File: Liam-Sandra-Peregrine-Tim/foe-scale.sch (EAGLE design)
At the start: 43 parts, among them U1 LM311, U2 SAMD21E

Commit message: finished up layout. Try to place all of the names and values of th components so that they do not overlap. To do so, use the smash command by typing smash and then clicking on the component. Xs will appear next to the component name and value, and thee will appear on the silk screen. Move them around so that none overlap and so that they are right next to the component that they correspond to. You can change the size of the text in properties if need be.
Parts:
- removed U$5: LMC6482, foe-scale:LMC6482
- removed U$9: RED_LED, foe-scale:RED_LED
- added 3.3V, 5V, AGND, DGND, HYS, INA_OUT: TEST_POINT, foe-scale:TEST_POINT
- added C10, C11: 1uF, rcl:C-EUC0805K
- renumbered U$4 to SIGNAL
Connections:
- removed net TESTTESTTEST: C4.2
- net +3V3: now also 3.3V.P$1, C11.1
- net +5V: now also 5V.P$1, C10.1
- net AGND: now also AGND.P$1, C10.2, C4.2
- net DGND: now also C11.2, DGND.P$1
- net N$16: now also U$3G$2.AIN+; no longer U$5G$1.AIN+
- net N$19: now also INA_OUT.P$1, U$3G$2.OUT; no longer U$5G$1.OUT
- net N$20: now also U$3G$2.AIN-; no longer U$5G$1.AIN-
- net N$27: now also HYS.P$1
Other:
- moved on the sheet: C4

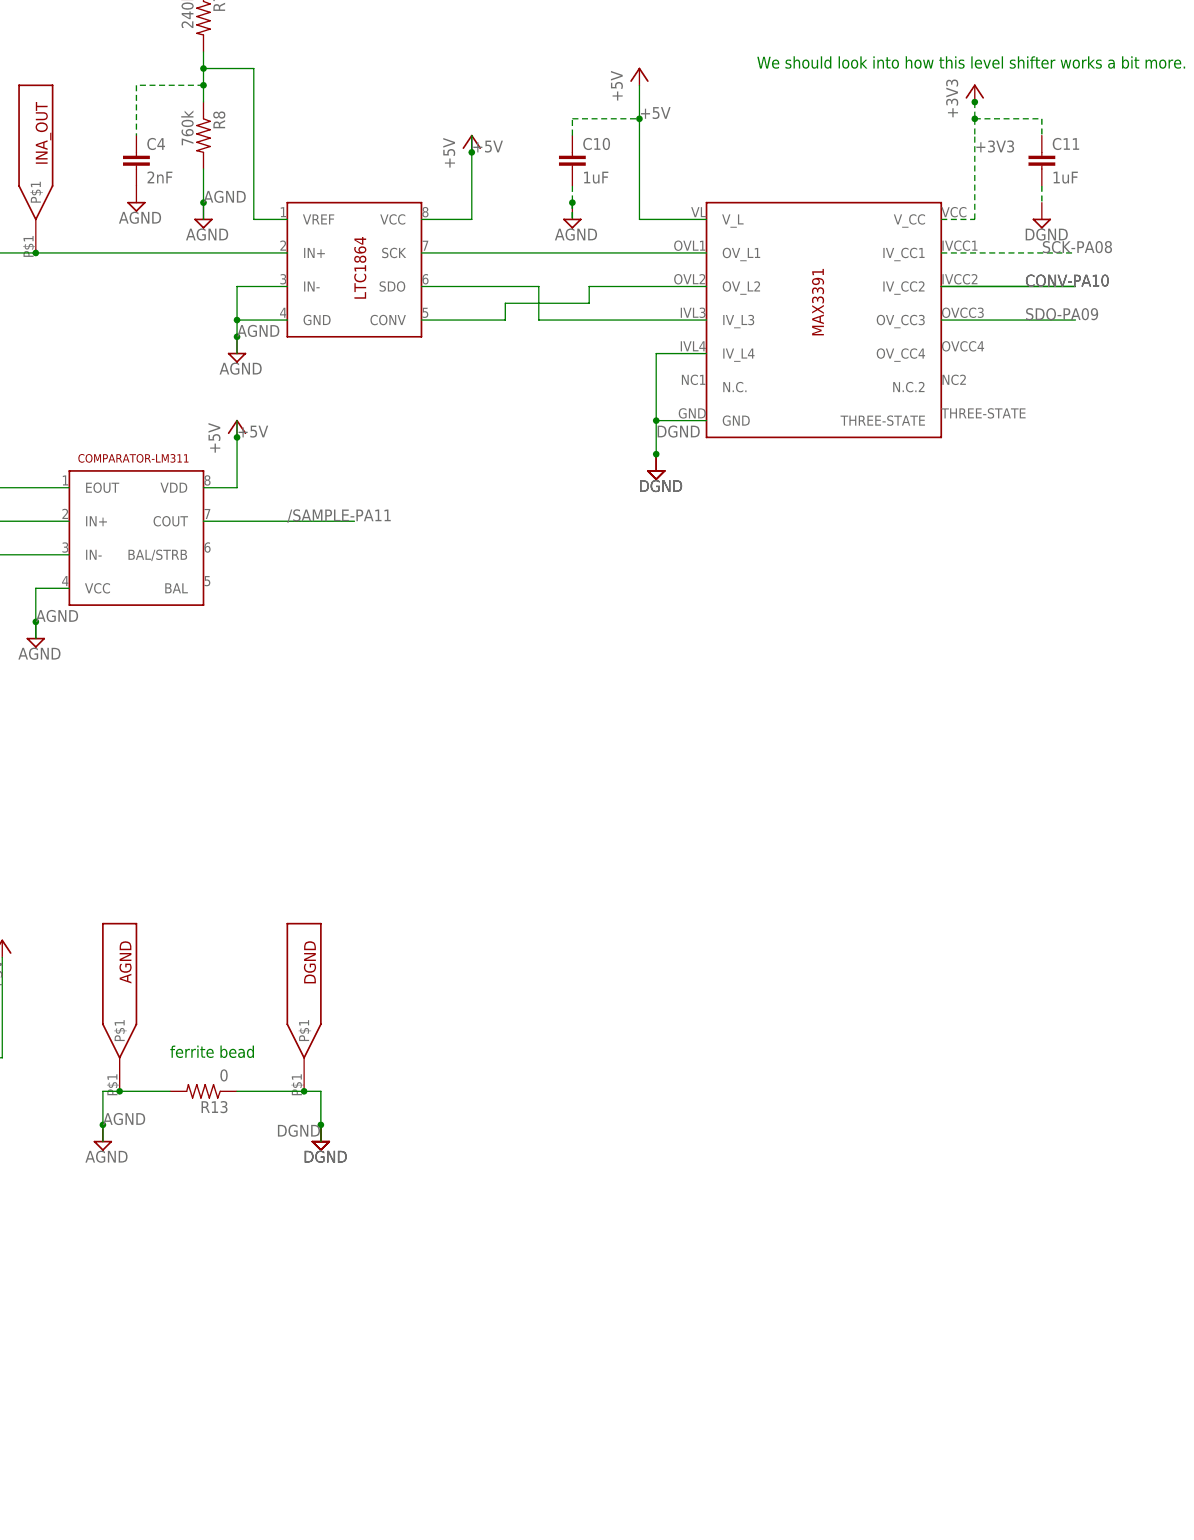
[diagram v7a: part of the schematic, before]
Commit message: replaced microUSB with standard USB B
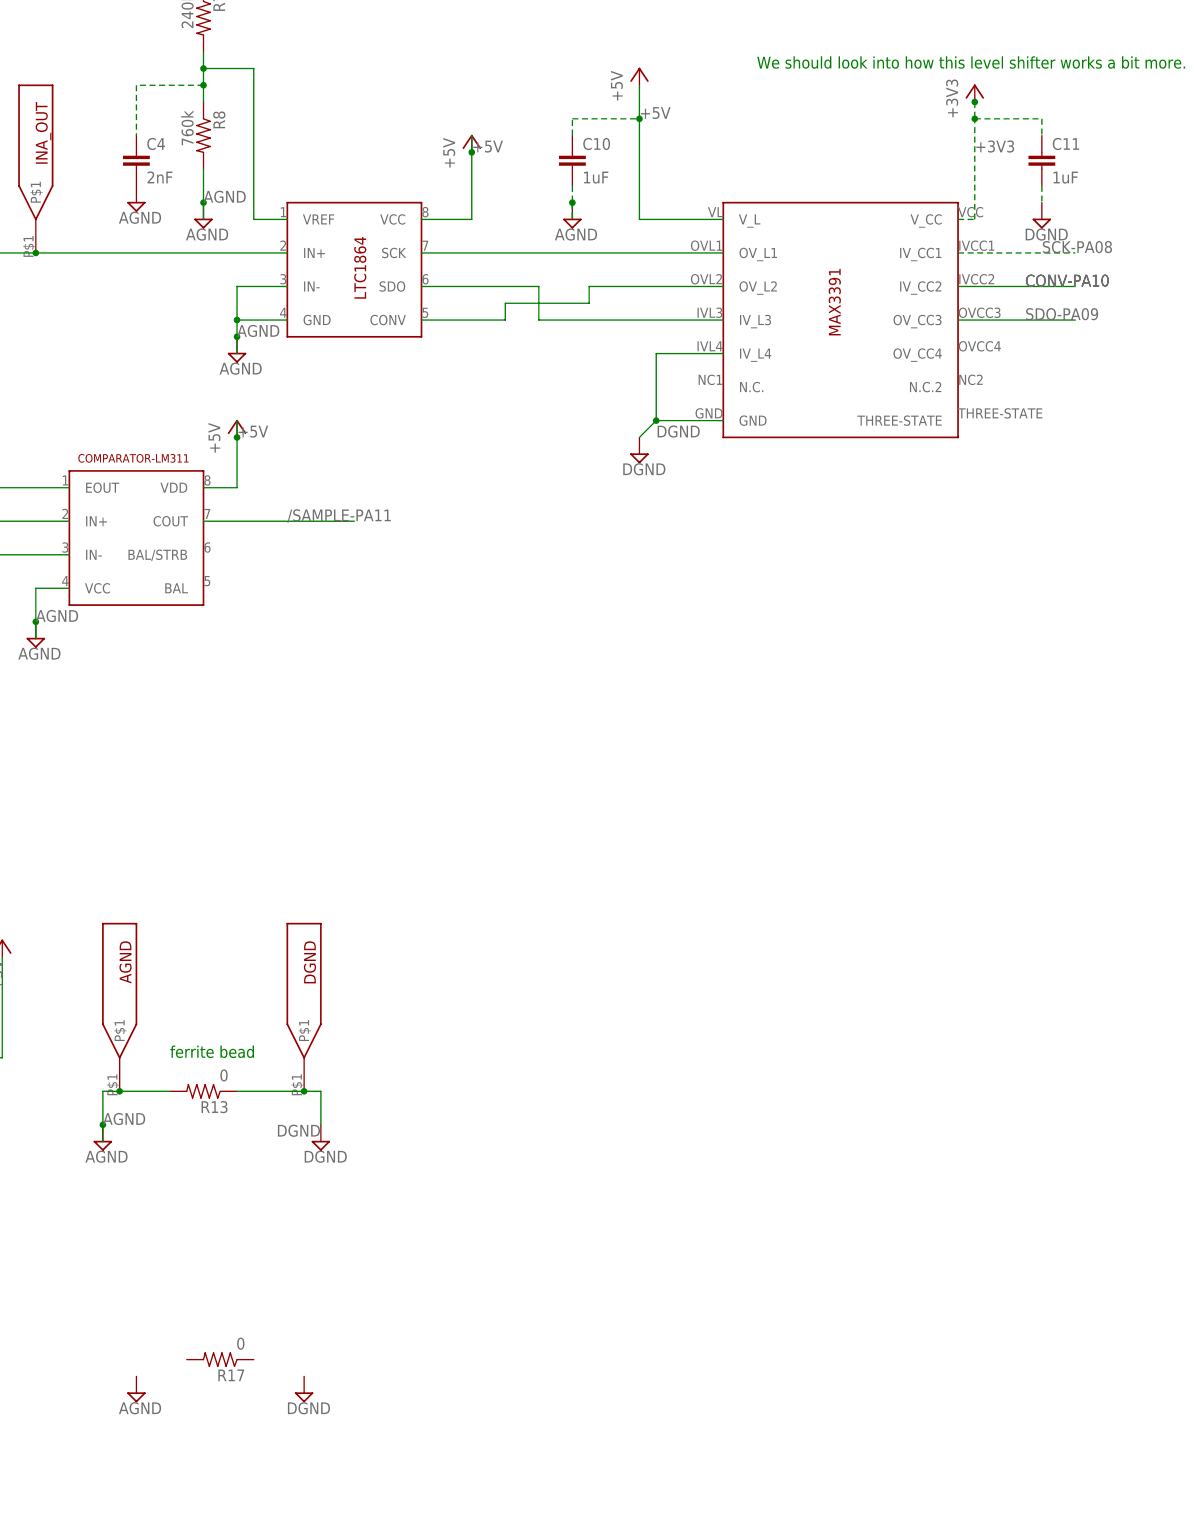
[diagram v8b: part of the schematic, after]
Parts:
- added R17: 0, resistor:R-US_R0805
